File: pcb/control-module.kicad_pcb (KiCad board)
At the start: 2 copper layers, 66 x 63.5 mm, 109 parts, among them J1 Screw_Terminal_01x06, J2 Conn_01x07_Pin, J3 USB_C_Receptacle_USB2.0_16P, J4 Micro_SD_Card, J5 Conn_ST_STDC14, J6 Conn_Coaxial, Q1 SiS454DN, Q2 SiS454DN, SW1 SW_DIP_x04, SW2 SW_DIP_x04, U1 TPS2116DRL, U2 USBLC6-2SC6, U3 STM32U545RETxQ, U4 MS5607-02BA, U5 LSM6DSL, U6 MCP73831-2-OT, U7 MIC5504-3.3YM5, U9 STM32WL55CCUx

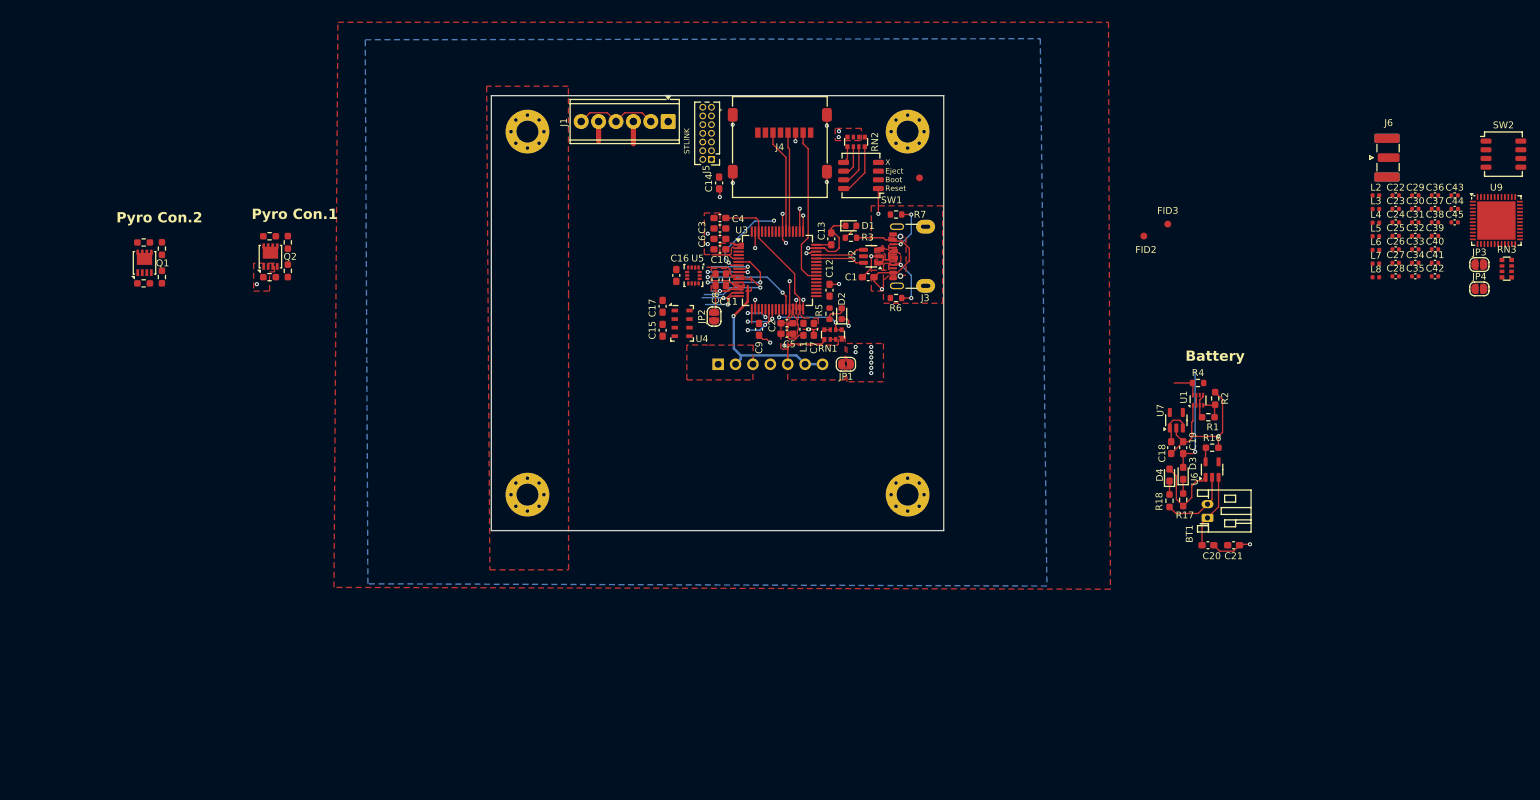
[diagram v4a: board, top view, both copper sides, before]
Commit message: Updated PCB Layout and routing
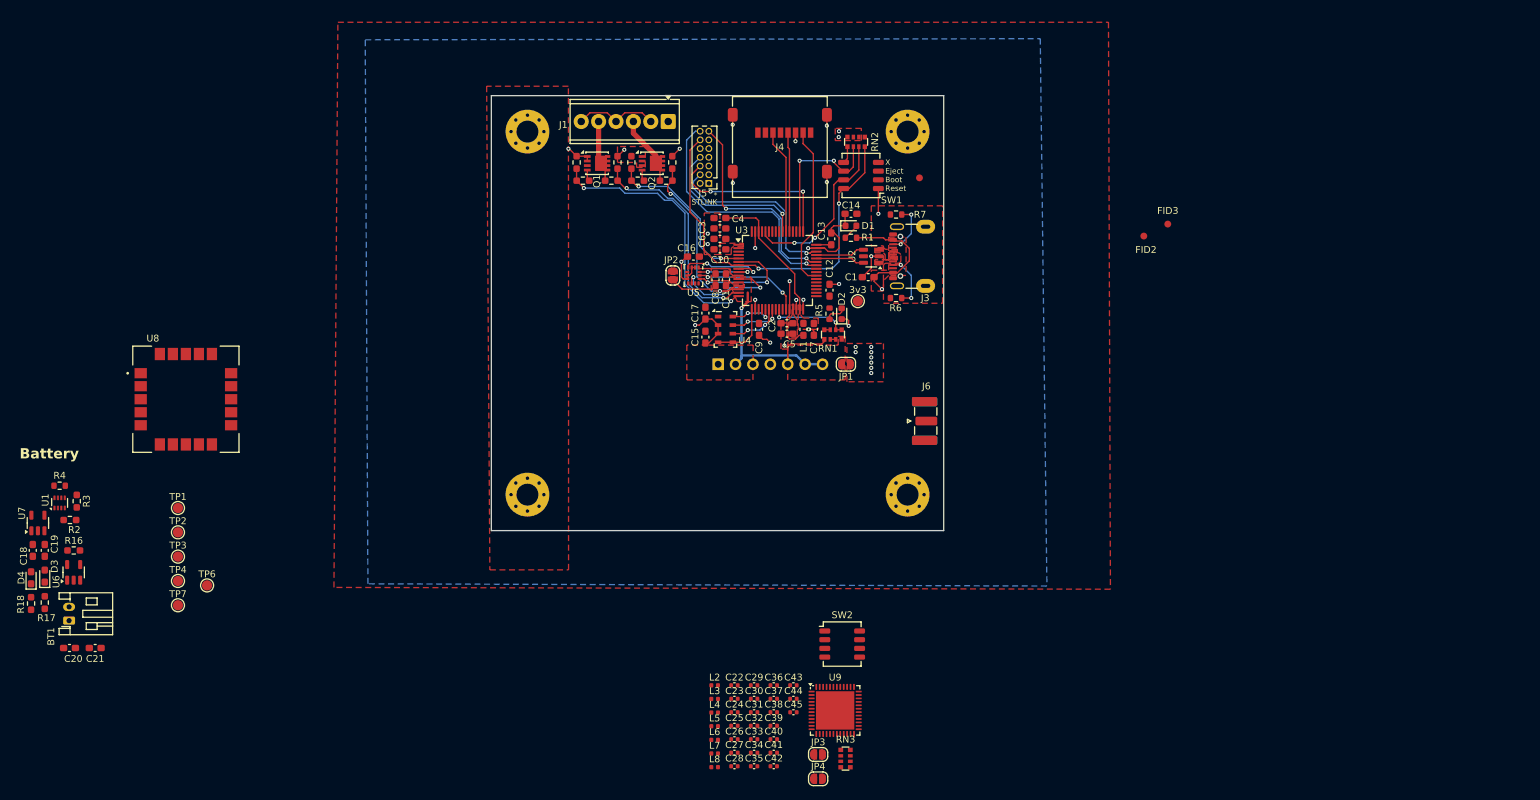
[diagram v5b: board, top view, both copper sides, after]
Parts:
- added 3v3: 3V3, TestPoint:TestPoint_Pad_D1.5mm, F.Cu at (169.0, 56.2)
- added TP1: GNDD, TestPoint:TestPoint_Pad_D1.5mm, F.Cu at (69.8, 86.5)
- added TP2: V_USB, TestPoint:TestPoint_Pad_D1.5mm, F.Cu at (69.8, 90.0)
- added TP3: V_{mux}, TestPoint:TestPoint_Pad_D1.5mm, F.Cu at (69.8, 93.5)
- added TP4: V_{BAT}, TestPoint:TestPoint_Pad_D1.5mm, F.Cu at (69.8, 97.1)
- added TP6: VDDUSB, TestPoint:TestPoint_Pad_D1.5mm, F.Cu at (74.0, 97.8)
- added TP7: GNDD, TestPoint:TestPoint_Pad_D1.5mm, F.Cu at (69.8, 100.7)
- added U8: SAM-M10Q-00B, SAM M10Q:XCVR_SAM-M10Q-00B, F.Cu at (70.9, 70.6)
- C37: value C -> 47nF
- C38, C41, C43: value C -> 68pF
- C39: value C -> 2.7pF
- C40: value C -> 15pF
- C42: value C -> 5.6pF
- C44, C45: value C -> 8.2pF
- L5: value L -> 56nH
- L6: value L -> 12nH
- L7: value L -> 20nH
- L8: value L -> 18nH
- moved BT1 166.9 mm to (53.9, 102.9)
- moved C18 166.9 mm to (50.3, 92.6)
- moved C19 166.9 mm to (48.6, 92.6)
- moved C20 166.9 mm to (53.9, 106.9)
- moved C21 166.9 mm to (57.7, 106.9)
- moved D3 166.9 mm to (50.3, 96.4)
- moved D4 166.9 mm to (48.3, 96.6)
- moved R17 166.9 mm to (50.3, 100.2)
- moved R18 166.9 mm to (48.3, 100.4)
- moved U6 166.9 mm to (54.5, 95.8)
- moved U7 166.9 mm to (49.3, 88.6)
- moved R16 166.9 mm to (54.5, 92.6)
- moved R2 166.9 mm to (54.0, 88.2)
- moved R3 166.9 mm to (55.0, 85.4)
- moved R4 166.9 mm to (52.5, 83.2)
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- renumbered R3 to R1, R1 to R2, R2 to R3
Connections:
- net /Transmitter/BOOT0 renamed /transmitter/BOOT0
- net /Transmitter/NRST renamed /transmitter/NRST
- net /Transmitter/OSC_IN renamed /transmitter/OSC_IN
- net /Transmitter/OSC_OUT renamed /transmitter/OSC_OUT
- BT1 pad 1: /Battery/V_{BAT} -> /V_{BAT}
- C19 pad 1: /Battery/V_{mux} -> /V_{mux}
- C20 pad 1: /Battery/V_{BAT} -> /V_{BAT}
- U6 pad 3: /Battery/V_{BAT} -> /V_{BAT}
- U7 pad 1: /Battery/V_{mux} -> /V_{mux}
- U7 pad 3: /Battery/V_{mux} -> /V_{mux}
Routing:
- net /NRST: track 20.4 -> 57.6 mm
- net /MCU/MCU_TX: track 0.00 -> 36.2 mm, vias 0 -> 1
- net /MCU/PYRO2_FIRE: track 5.74 -> 39.3 mm, vias 1 -> 2
- net /MCU/MCU_RX: track 0.00 -> 31.5 mm, vias 0 -> 2
- net /MCU/ADC1_IN6: track 5.67 -> 32.8 mm, vias 1 -> 2
- net /MCU/SWDIO: track 1.54 -> 27.4 mm
- net /MCU/SWCLK: track 2.34 -> 25.6 mm, vias 1 -> 2
- net /MCU/ADC1_IN5: track 4.11 -> 25.1 mm, vias 1 -> 2
- net /MCU/PYRO1_FIRE: track 4.12 -> 24.4 mm, vias 0 -> 2
- net /BOOT0: track 6.23 -> 25.4 mm, vias 0 -> 2
- net GNDD: track 83.6 -> 65.2 mm, vias 33 -> 34
- net /MCU/SWO: track 4.46 -> 22.9 mm, vias 2 -> 1
- net +5V_USB: track 34.1 -> 18.5 mm, vias 2 -> 1
- net /SD_EJECT: track 7.98 -> 22.2 mm, vias 1 -> 2
- net /Battery/Status: track 12.2 -> 0.00 mm
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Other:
- board text added: "Control Module Rev. 2"
- board text removed: "Control Module Testbed"
- board text removed: "Pyro Con.1"
- board text removed: "Pyro Con.2"

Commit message: Updated PCB Layout, changed to 4 layer board
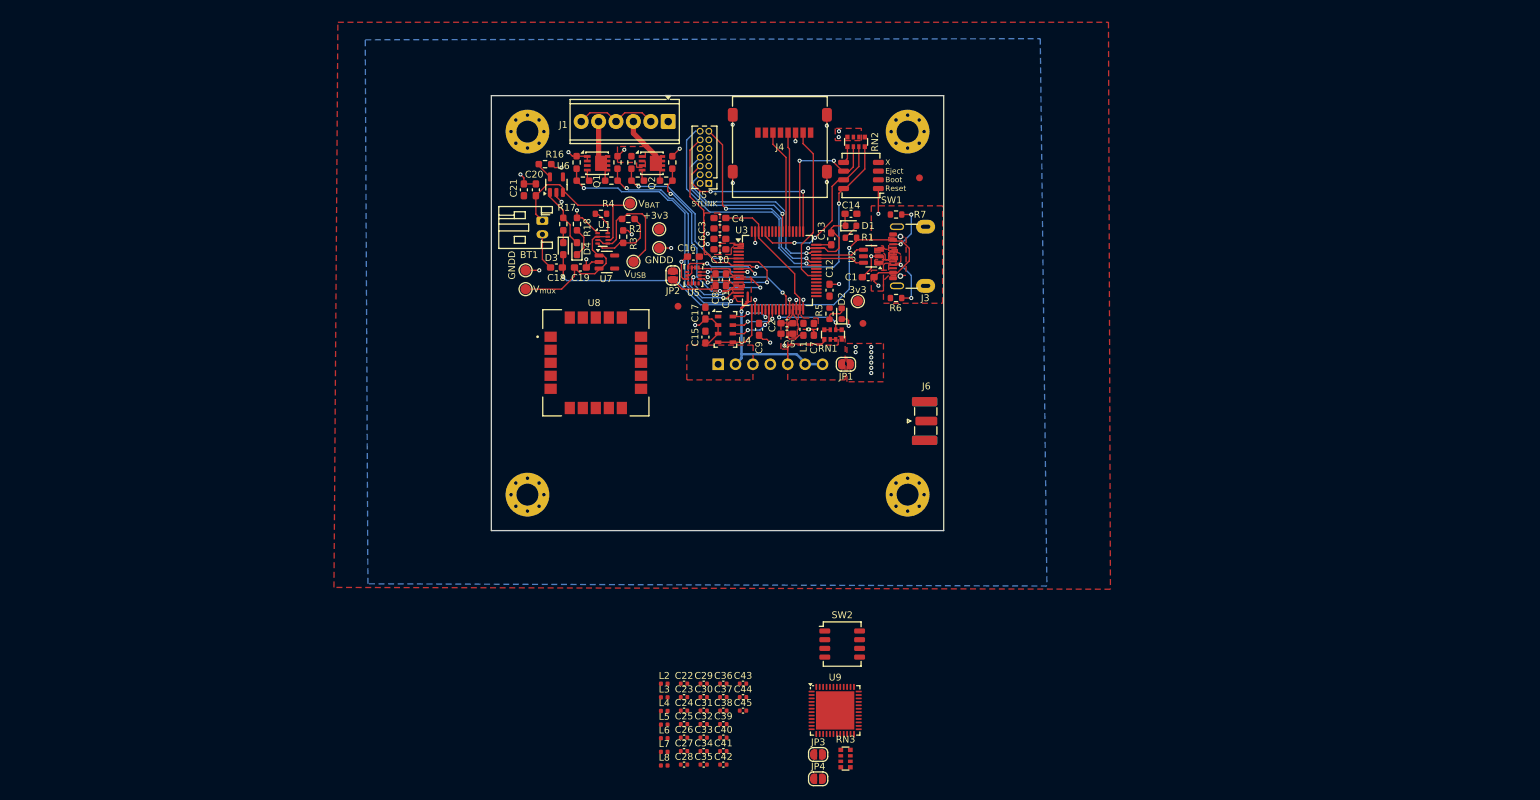
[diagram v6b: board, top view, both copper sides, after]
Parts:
- moved R18 97.1 mm to (128.0, 45.0), turned to 90 degrees
- moved C20 95.4 mm to (122.0, 40.0), turned to 90 degrees
- moved R17 93.7 mm to (126.0, 45.0), turned to 90 degrees
- moved D4 93.1 mm to (128.0, 48.6)
- moved R2 92.6 mm to (135.5, 44.2)
- moved C21 91.6 mm to (120.2, 40.0), turned to 90 degrees
- moved U7 91.4 mm to (132.4, 50.5), turned to 0 degrees
- moved BT1 90.5 mm to (123.0, 44.5), turned to -90 degrees
- moved U6 90.4 mm to (125.0, 39.2)
- moved C19 90.0 mm to (128.5, 51.3), turned to 0 degrees
- moved D3 89.5 mm to (126.0, 48.6), turned to -90 degrees
- moved R16 89.0 mm to (123.3, 36.2)
- moved R3 88.6 mm to (134.8, 46.8)
- moved R4 88.4 mm to (131.5, 43.5)
- moved U1 88.2 mm to (131.8, 47.1), turned to 0 degrees
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- renumbered TP6 to +3v3, TP1 to GNDD, TP7 to GNDD, TP4 to V_{BAT}, TP2 to V_{USB}, TP3 to V_{mux}
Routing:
- net +5V_USB: track 18.5 -> 73.5 mm, vias 1 -> 3
- net /V_{BAT}: track 0.00 -> 25.8 mm
- net GNDD: track 65.2 -> 89.9 mm, vias 34 -> 42
- net /V_{mux}: track 0.00 -> 22.1 mm
- net /V_USB: track 0.00 -> 17.8 mm
- net Net-(U1-PR1): track 0.00 -> 10.2 mm
- net /Battery/Status: track 0.00 -> 8.98 mm
- net Net-(D4-K): track 0.00 -> 4.38 mm
- net Net-(U1-ST): track 0.00 -> 3.33 mm
- net Net-(U3-VLXSMPS): track 11.6 -> 8.92 mm
- net /Battery/Program: track 0.00 -> 2.54 mm
- net Net-(D3-K): track 0.00 -> 1.80 mm
- net /IMU Sensors/imu_int1: track 12.8 -> 13.5 mm
- net /NRST: track 57.6 -> 57.1 mm
- net /MCU/MCU_TX: track 36.2 -> 35.7 mm
- removed copper zone on F.Cu, net Net-(J1-Pin_2)
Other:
- copper layers 2 -> 4
- board text added: "3v3"
- board text added: "P1"
- board text added: "P2"
- board text added: "X"
- board text removed: "Battery"
- board text removed: "P1+"
- board text removed: "P1-"
- board text removed: "P2+"
- board text removed: "P2-"
- board text removed: "V+"
- board text removed: "V-"

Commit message: Updated Board size and layout
Full Layout of Rev 2 board, without RF shield and other updates.
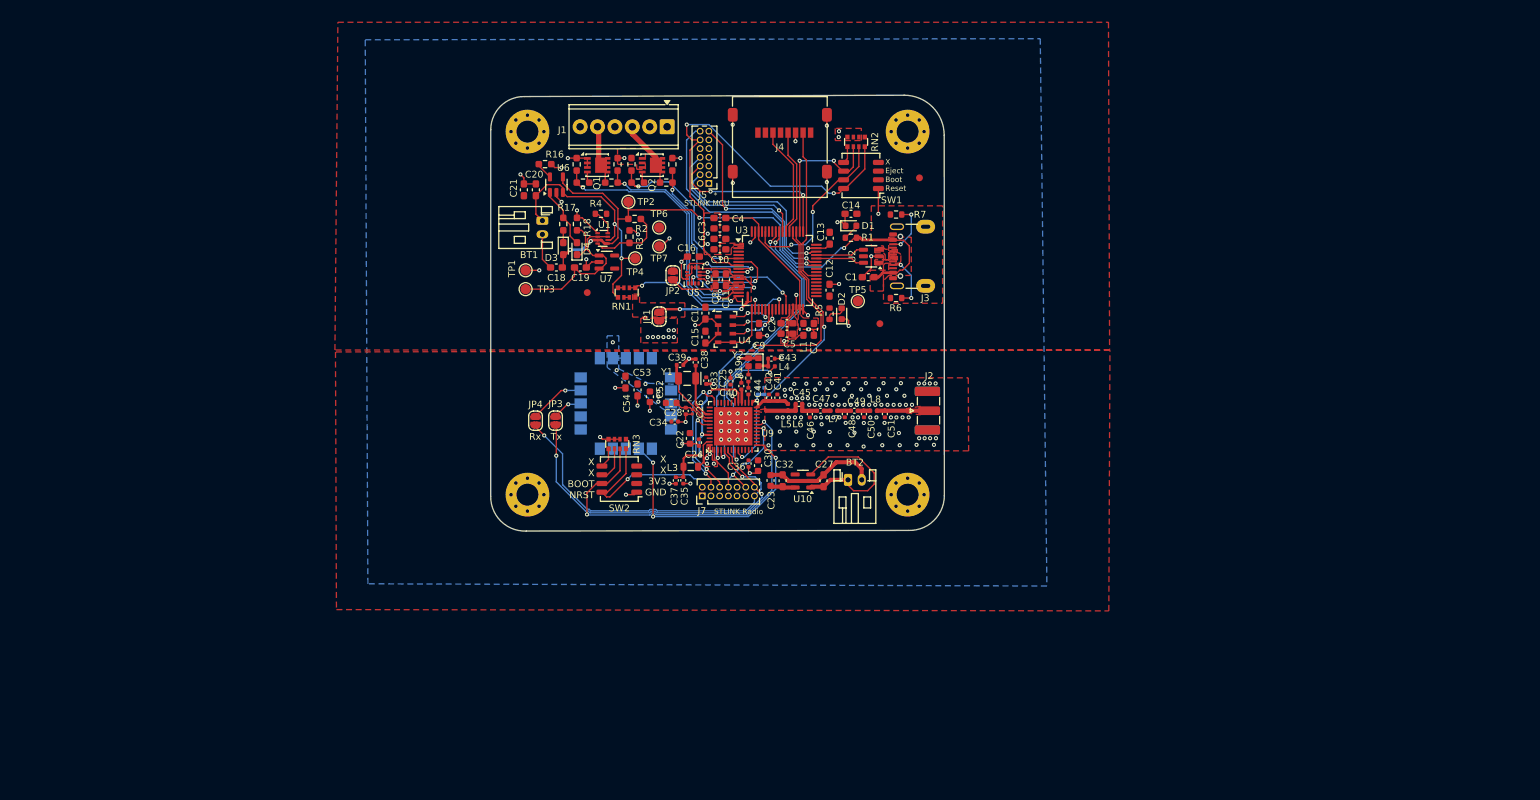
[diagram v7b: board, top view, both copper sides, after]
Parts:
- removed J6: Conn_Coaxial, Connector_Coaxial:SMA_Samtec_SMA-J-P-H-ST-EM1_EdgeMount
- added BT2: Battery_Cell, Connector_JST:JST_PH_S2B-PH-K_1x02_P2.00mm_Horizontal, F.Cu at (167.6, 82.3)
- added C46: 15pF, Capacitor_SMD:C_0402_1005Metric, F.Cu at (162.0, 72.8)
- added C47: 68pF, Capacitor_SMD:C_0402_1005Metric, F.Cu at (163.6, 72.2)
- added C48: 5.6pF, Capacitor_SMD:C_0402_1005Metric, F.Cu at (167.1, 72.7)
- added C49: 68pF, Capacitor_SMD:C_0402_1005Metric, F.Cu at (168.5, 72.2)
- added C50: 6.8pF, Capacitor_SMD:C_0402_1005Metric, F.Cu at (169.9, 72.7)
- added C51: 6.8pF, Capacitor_SMD:C_0402_1005Metric, F.Cu at (172.9, 72.7)
- added C52: 4.7uF, Capacitor_SMD:C_0603_1608Metric, F.Cu at (138.7, 70.2)
- added C53: 100nF, Capacitor_SMD:C_0603_1608Metric_Pad1.08x0.95mm_HandSolder, F.Cu at (136.8, 69.2)
- added C54: 1uF, Capacitor_SMD:C_0603_1608Metric_Pad1.08x0.95mm_HandSolder, F.Cu at (135.1, 68.1)
- added J7: Conn_ST_STDC14, Connector_PinHeader_1.27mm:PinHeader_2x07_P1.27mm_Vertical, F.Cu at (146.3, 84.7)
- added R19: 220R, Resistor_SMD:R_0402_1005Metric, F.Cu at (153.0, 67.5)
- added U10: MIC5504-3.3YM5, Package_TO_SOT_SMD:SOT-23-5, F.Cu at (161.0, 82.5)
- added Y1: Crystal, Crystal:Crystal_SMD_G8-2Pin_3.2x1.5mm, F.Cu at (144.1, 67.5)
- added Y2: Crystal_GND23, Crystal:Crystal_SMD_SeikoEpson_FA128-4Pin_2.0x1.6mm, F.Cu at (153.8, 65.2)
- C22, C23, C30: value C -> 4.7uF; footprint Capacitor_SMD:C_0402_1005Metric -> Capacitor_SMD:C_0603_1608Metric
- C24, C28, C33, C34, C36: value C -> 100nF
- C25: value C -> 33pF
- C26: value C -> 4.7uF; footprint Capacitor_SMD:C_0402_1005Metric -> Capacitor_SMD:C_0201_0603Metric
- C27, C32: value C -> 1uF; footprint Capacitor_SMD:C_0402_1005Metric -> Capacitor_SMD:C_0603_1608Metric_Pad1.08x0.95mm_HandSolder
- C29: value C -> 33pF; moved to B.Cu
- C31: value C -> 100nF; moved to B.Cu
- C35: value C -> 0.47uF
- C37: value 47nF -> 33pF
- C38: value 68pF -> 6.8pF
- C39: value 2.7pF -> 6.8pF
- C40: value 15pF -> 100nF
- C41: value 68pF -> 47nF
- C42: value 5.6pF -> 68pF
- C43: value 68pF -> 220nF
- C44: value 8.2pF -> 10pF
- C45: value 8.2pF -> 4.3pF
- J2: value Conn_01x07_Pin -> Conn_Coaxial; footprint Connector_PinHeader_2.54mm:PinHeader_1x07_P2.54mm_Vertical -> Connector_Coaxial:SMA_Samtec_SMA-J-P-H-ST-EM1_EdgeMount; moved to F.Cu
- L2: value L -> 600R Ferrite Bead; footprint Inductor_SMD:L_0402_1005Metric -> Inductor_SMD:L_0603_1608Metric
- L3: value L -> 15uH; footprint Inductor_SMD:L_0402_1005Metric -> Inductor_SMD:L_0805_2012Metric
- L4: value L -> 1400R Ferrite Bead
- L6: value 12nH -> 6.8nH
- L7: value 20nH -> 16nH
- L8: value 18nH -> 16nH
- TP2: renamed from V_{USB}; value V_USB -> +5V_{USB}
- U8: moved to B.Cu
- moved JP4 66.6 mm to (122.0, 73.7), turned to 90 degrees
- moved JP3 62.0 mm to (124.9, 73.7), turned to -90 degrees
- moved L8 60.1 mm to (171.3, 72.2)
- moved RN3 56.7 mm to (133.9, 77.1), turned to -90 degrees
- moved L7 55.6 mm to (165.5, 72.2)
- moved C42 54.0 mm to (156.1, 70.3), turned to 90 degrees
- moved C39 52.8 mm to (143.0, 65.6), turned to 180 degrees
- moved L4 52.7 mm to (156.4, 65.8)
- moved C41 52.2 mm to (157.2, 70.3), turned to 90 degrees
- moved C33 52.1 mm to (146.9, 67.9), turned to -90 degrees
- moved L6 51.7 mm to (160.4, 72.2)
- moved C28 51.6 mm to (143.9, 72.3), turned to -90 degrees
- moved C40 51.4 mm to (152.0, 68.7), turned to 90 degrees
- moved C38 51.0 mm to (145.3, 65.2), turned to -90 degrees
- moved C25 50.5 mm to (150.4, 68.0), turned to 90 degrees
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- renumbered GNDD to TP1, V_{mux} to TP3, V_{BAT} to TP4, 3v3 to TP5, +3v3 to TP6, GNDD to TP7
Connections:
- net /transmitter/BOOT0 renamed /transmitter/BOOT0_radio
- net /transmitter/NRST renamed /NRST_radio
- BT1 pad 1: /V_{BAT} -> V_{BAT}
- C20 pad 1: /V_{BAT} -> V_{BAT}
- C22 pad 1: Net-(U9-VDDPA) -> +3.3V_radio
- C23 pad 1: Net-(U9-VDDPA) -> +3.3V_radio
- C24 pad 1: Net-(U9-VDDA) -> +3.3V_radio
- C25 pad 1: Net-(U9-VDDA) -> +3.3V_radio
- C26 pad 1: +3.3V -> Net-(U9-VDDA)
- C27 pad 1: +3.3V -> /transmitter/V_{battery_radio}
- C28 pad 1: /transmitter/OSC_IN -> Net-(U9-VDDA)
- C29 pad 1: +3.3V -> +3.3V_radio
- C30 pad 1: Net-(U9-VDDRF1V55) -> +3.3V_radio
- C31 pad 1: GNDD -> +3.3V_radio
- C31 pad 2: Net-(U9-PC15) -> GNDD
- C32 pad 1: /transmitter/OSC_OUT -> +3.3V_radio
- C33 pad 1: +3.3V -> +3.3V_radio
- C34 pad 1: Net-(U9-VDDRF1V55) -> +3.3V_radio
- C35 pad 1: +3.3V -> VDDRF1V55
- C36 pad 1: GNDD -> +3.3V_radio
- C36 pad 2: Net-(U9-PC14) -> GNDD
- C37 pad 1: Net-(U9-VR_PA) -> VDDRF1V55
- C38 pad 1: Net-(U9-VR_PA) -> GNDD
- C38 pad 2: GNDD -> Net-(U9-PC14)
- C39 pad 1: Net-(C39-Pad1) -> GNDD
- C39 pad 2: Net-(C39-Pad2) -> Net-(U9-PC15)
- C40 pad 1: Net-(C39-Pad2) -> +3.3V_radio
- C41 pad 1: Net-(C41-Pad1) -> Net-(U9-VR_PA)
- C41 pad 2: Net-(C39-Pad2) -> GNDD
- C42 pad 1: Net-(C42-Pad1) -> Net-(U9-VR_PA)
- C43 pad 1: Net-(C42-Pad1) -> Net-(C43-Pad1)
- C43 pad 2: Net-(C43-Pad2) -> GNDD
- C44 pad 1: Net-(C43-Pad2) -> /transmitter/OSC_IN
- C44 pad 2: GNDD -> Net-(C44-Pad2)
- C45 pad 1: Net-(J6-In) -> Net-(U9-RFO_HP)
- C45 pad 2: GNDD -> Net-(C45-Pad2)
- J1 pad 2: Net-(J1-Pin_2) -> unconnected-(J1-Pin_2-Pad2)
- J1 pad 4: Net-(J1-Pin_2) -> unconnected-(J1-Pin_4-Pad4)
- J1 pad 6: Net-(J1-Pin_2) -> +3.3V
- J2 pad 1: GNDA -> Net-(J2-In)
- J2 pad 2: GNDA -> GNDD
- JP3 pad 1: GNDD -> /Ublox_GPS_module/GPS_TX
- JP3 pad 2: GNDA -> /radio_TX
- JP4 pad 1: +3.3V -> /radio_RX
- JP4 pad 2: VDDA -> /Ublox_GPS_module/GPS_RX
- L2 pad 2: +3.3V -> +3.3V_radio
- L3 pad 2: Net-(U9-VDDRF1V55) -> VDDRF1V55
- L4 pad 1: Net-(U9-RFO_HP) -> Net-(C43-Pad1)
- L4 pad 2: Net-(C39-Pad1) -> /transmitter/VDD_TCXO
- L5 pad 2: Net-(C39-Pad1) -> Net-(U9-RFO_HP)
- L6 pad 1: Net-(C39-Pad1) -> Net-(U9-RFO_HP)
- L6 pad 2: Net-(C39-Pad2) -> Net-(C45-Pad2)
- L7 pad 1: Net-(C41-Pad1) -> Net-(C47-Pad1)
- L7 pad 2: Net-(C42-Pad1) -> Net-(C48-Pad1)
- L8 pad 1: Net-(C43-Pad2) -> Net-(C49-Pad2)
- L8 pad 2: Net-(J6-In) -> Net-(J2-In)
- R2 pad 2: /V_USB -> +5V_USB
- RN1 pad 1: +BATT -> V_{BAT}
- RN3 pad 1: +3.3V -> +3.3V_radio
- SW2 pad 2: +3.3V -> +3.3V_radio
- TP2 pad 1: /V_USB -> +5V_USB
- TP4 pad 1: /V_{BAT} -> V_{BAT}
- U1 pad 3: /V_USB -> +5V_USB
- U1 pad 5: /V_USB -> +5V_USB
- U1 pad 6: /V_{BAT} -> V_{BAT}
- U3 pad 51: unconnected-(U3-PC10-Pad51) -> /SPI3_SCK
- U3 pad 52: unconnected-(U3-PC11-Pad52) -> /SPI3_MISO
- U3 pad 56: unconnected-(U3-PB4-Pad56) -> /SPI3_CS
- U3 pad 57: unconnected-(U3-PB5-Pad57) -> /SPI3_MOSI
- U6 pad 3: /V_{BAT} -> V_{BAT}
- U6 pad 4: /Battery/V_USB -> +5V_USB
- U8 pad 1: GND -> GNDD
- U8 pad 10: GND -> GNDD
- U8 pad 11: GND -> GNDD
- U8 pad 13: unconnected-(U8-TXD-Pad13) -> /Ublox_GPS_module/GPS_TX
- U8 pad 14: unconnected-(U8-RXD-Pad14) -> /Ublox_GPS_module/GPS_RX
- U8 pad 15: GND -> GNDD
- U8 pad 16: GND -> GNDD
- U8 pad 17: unconnected-(U8-VCC-Pad17) -> +3.3V_radio
- U8 pad 18: unconnected-(U8-~{RESET}-Pad18) -> +3.3V_radio
- U8 pad 2: unconnected-(U8-V_IO-Pad2) -> +3.3V_radio
- U8 pad 20: GND -> GNDD
- U8 pad 3: unconnected-(U8-V_BCKP-Pad3) -> +3.3V_radio
- U8 pad 4: GND -> GNDD
- U8 pad 5: GND -> GNDD
- U8 pad 6: GND -> GNDD
- U8 pad 7: unconnected-(U8-TIMEPULSE-Pad7) -> /Ublox_GPS_module/TIMEPULSE_OUT
- U9 pad 1: unconnected-(U9-PB3-Pad1) -> /SWO_radio
- U9 pad 11: +3.3V -> +3.3V_radio
- U9 pad 13: unconnected-(U9-PA5-Pad13) -> /Ublox_GPS_module/TIMEPULSE_OUT
- U9 pad 2: unconnected-(U9-PB4-Pad2) -> /SPI3_MISO
- U9 pad 25: Net-(U9-VDDPA) -> +3.3V_radio
- U9 pad 27: /transmitter/OSC_OUT -> unconnected-(U9-OSC_OUT-Pad27)
- U9 pad 28: Net-(U9-VDDPA) -> +3.3V_radio
- U9 pad 29: Net-(U9-VDDRF1V55) -> VDDRF1V55
- U9 pad 3: unconnected-(U9-PB5-Pad3) -> /SPI3_MOSI
- U9 pad 30: unconnected-(U9-PB0-Pad30) -> /transmitter/VDD_TCXO
- U9 pad 36: unconnected-(U9-PA13-Pad36) -> /SWDIO_radio
- U9 pad 37: +3.3V -> +3.3V_radio
- U9 pad 4: unconnected-(U9-PB6-Pad4) -> /radio_RX
- U9 pad 42: unconnected-(U9-PA14-Pad42) -> /SWCLK_radio
- U9 pad 44: +3.3V -> +3.3V_radio
- U9 pad 45: Net-(U9-VDDRF1V55) -> VDDRF1V55
- U9 pad 46: Net-(U9-VDDPA) -> +3.3V_radio
- U9 pad 5: unconnected-(U9-PB7-Pad5) -> /radio_TX
- U9 pad 7: unconnected-(U9-PA0-Pad7) -> /SPI3_CS
- U9 pad 8: unconnected-(U9-PA1-Pad8) -> /SPI3_SCK
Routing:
- net /transmitter/BOOT0_radio: track 0.00 -> 52.9 mm, vias 0 -> 2
- net /radio_RX: track 0.00 -> 52.0 mm, vias 0 -> 2
- net /radio_TX: track 0.00 -> 50.4 mm, vias 0 -> 2
- net /SPI3_MISO: track 0.00 -> 48.3 mm, vias 0 -> 2
- net /NRST_radio: track 0.00 -> 42.1 mm, vias 0 -> 3
- net /SPI3_CS: track 0.00 -> 42.0 mm, vias 0 -> 2
- net /SPI3_MOSI: track 0.00 -> 41.2 mm, vias 0 -> 2
- net /SPI3_SCK: track 0.00 -> 41.0 mm, vias 0 -> 2
- net GNDD: track 89.9 -> 129.3 mm, vias 42 -> 171
- net /Ublox_GPS_module/TIMEPULSE_OUT: track 0.00 -> 38.5 mm, vias 0 -> 3
- net V_{BAT}: track 0.00 -> 37.1 mm, vias 0 -> 2
- net /V_{BAT}: track 25.8 -> 0.00 mm
- net /transmitter/V_{battery_radio}: track 0.00 -> 24.2 mm
- net VDDRF1V55: track 0.00 -> 23.3 mm, vias 0 -> 3
- net /SWDIO_radio: track 0.00 -> 18.3 mm, vias 0 -> 2
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- added copper zone on F.Cu, net (none)
- added copper zone on B.Cu, net +3.3V_radio
- added copper zone on F.Cu, net +3.3V_radio
- added copper zone on F.Cu, net +5V_USB
- added copper zone on F.Cu, net Net-(U9-RFO_HP)
- removed copper zone on F.Cu, net /V_USB
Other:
- board size 66 x 63.5 mm -> 66.2 x 63.6 mm
- copper layers 4 -> 2
- board text added: "Control Module Rev. 2 Electric Boogaloo"
- board text added: "Rx"
- board text added: "STLINK MCU"
- board text added: "STLINK Radio"
- board text added: "Tx"
- board text added: "X X 3V3 GND"
- board text added: "X X BOOT NRST"
- board text removed: "+3.3V"
- board text removed: "BAT+"
- board text removed: "Control Module Rev. 2"
- board text removed: "GNDA"
- board text removed: "STLINK"
